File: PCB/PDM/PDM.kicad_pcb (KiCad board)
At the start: 2 copper layers, 196 parts, among them IC1 BTS70021EPPXUMA1, IC1 STM32L496ZGT6, IC10 BTS70021EPPXUMA1, IC11 BTS70021EPPXUMA1, IC12 LM5050MK-1_NOPB, IC13 LM5050MK-1_NOPB, IC14 TLE9104SHXUMA1, IC2 AT25SF128A-SHB-T, IC2 BTS70021EPPXUMA1, IC3 BTS500101TAEATMA1, IC4 TS5A21366DCUR, IC5 TMP126NDCKR, IC6 TMP126NDCKR, IC7 BTS722204ESAXUMA1, IC8 BTS722204ESAXUMA1, IC9 BTS500101TAEATMA1, Q1 MMBT3904, Q2 IAUA250N04S6N007AUMA1, Q3 IAUA250N04S6N007AUMA1, Q4 NDT3055L, U1 STM32L496VGTx, U2 MCP2561-E-SN, U3 MCP2561-E-SN, U4 VNF1048FTR, Y1 48Mhz, Y2 32KHz

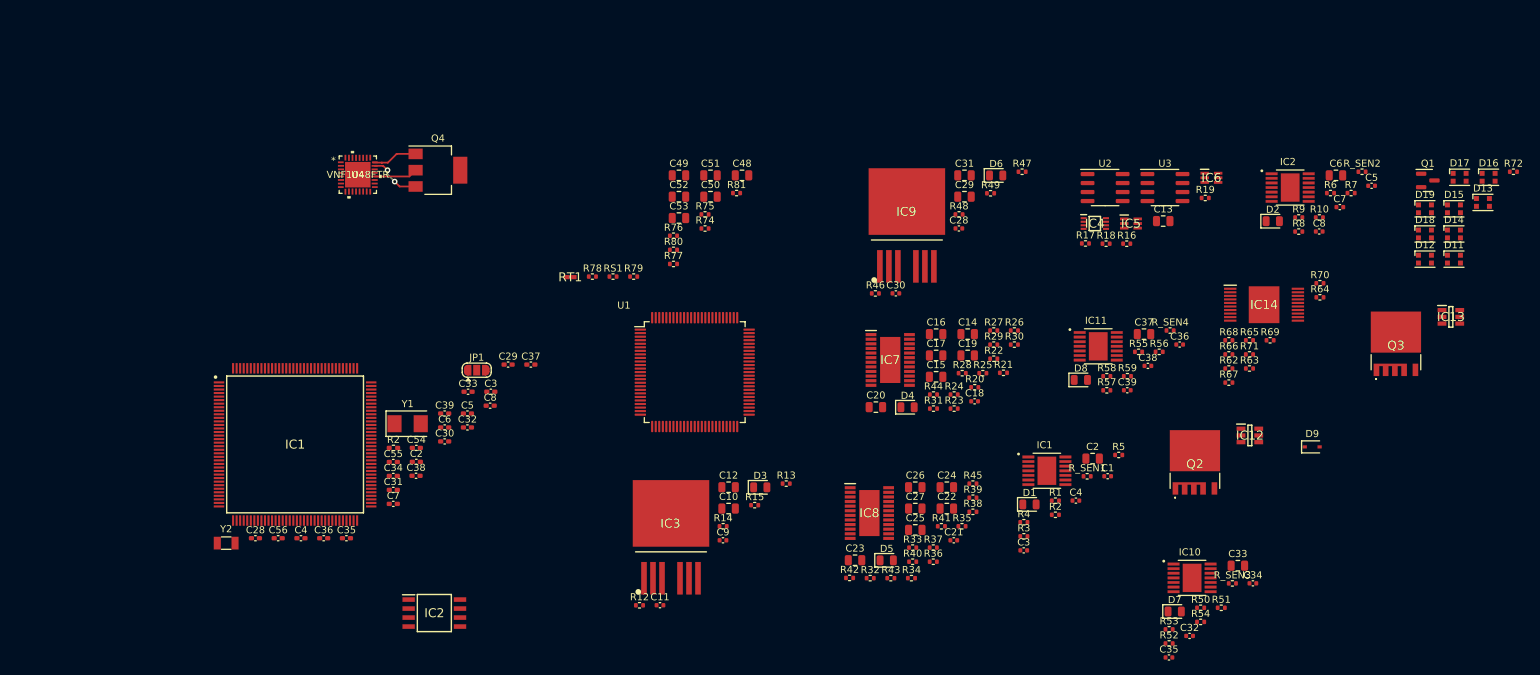
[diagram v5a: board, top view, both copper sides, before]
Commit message: Added new type of high side driver based on VNF1048 + STL135
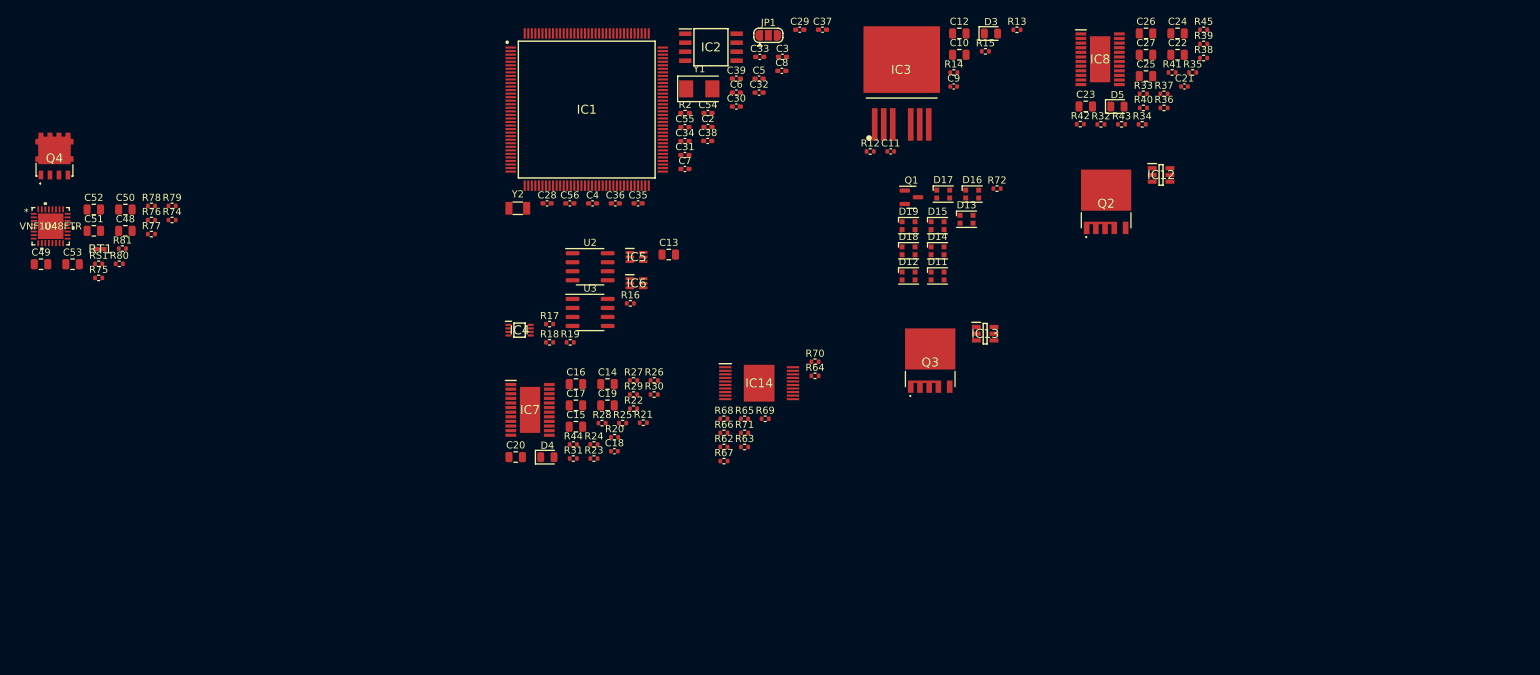
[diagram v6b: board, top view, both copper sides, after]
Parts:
- removed C1: 220pF, Capacitor_SMD:C_0402_1005Metric
- removed the C2 at (187.9, 89.0)
- removed the C2 at (92.5, 89.4)
- removed the C28 at (169.0, 56.5)
- removed the C28 at (69.8, 100.2)
- removed the C29 at (169.8, 52.0)
- removed the C29 at (105.4, 75.7)
- removed the C3 at (178.2, 101.9)
- removed the C3 at (103.0, 79.5)
- removed the C30 at (160.1, 65.6)
- removed the C30 at (96.5, 86.5)
- removed the C31 at (169.8, 49.0)
- removed the C31 at (89.2, 93.4)
- removed the C32 at (99.7, 84.6)
- removed the C32 at (201.6, 114.0)
- removed the C33 at (208.4, 104.1)
- removed the C33 at (99.8, 79.5)
- removed the C34 at (89.2, 91.4)
- removed the C34 at (210.5, 106.5)
- removed the C35 at (198.6, 117.0)
- removed the C35 at (82.6, 100.2)
- removed the C36 at (200.2, 72.9)
- removed the C36 at (79.4, 100.2)
- removed the C37 at (195.1, 71.4)
- removed the C37 at (108.6, 75.7)
- removed the C38 at (195.7, 75.9)
- removed the C38 at (92.4, 91.4)
- removed the C39 at (192.8, 79.3)
- removed the C39 at (96.5, 82.6)
- removed the C4 at (185.5, 94.9)
- removed the C4 at (76.2, 100.2)
- removed the C5 at (227.2, 50.5)
- removed the C5 at (99.7, 82.6)
- removed the C6 at (96.5, 84.6)
- removed the C6 at (222.2, 49.0)
- removed the C7 at (89.2, 95.3)
- removed the C7 at (222.8, 53.5)
- removed the C8 at (219.8, 56.9)
- removed the C8 at (102.9, 81.5)
- removed D1, D2, D7, D8: 7V, Diode_SMD:D_0805_2012Metric
- removed D6: 40V, Diode_SMD:D_0805_2012Metric
- removed D9: 5.1V, Diode_SMD:D_SOD-323
- removed the IC1 at (75.4, 87.0)
- removed the IC1 at (181.4, 90.7)
- removed IC10, IC11: BTS70021EPPXUMA1, PDM_Additional:SOP65P600X115-15N
- removed the IC2 at (215.7, 50.7)
- removed the IC2 at (95.0, 110.7)
- removed IC9: BTS500101TAEATMA1, PDM_Additional:PG-TO263-7-3_3
- removed R1, R50, R55, R6: 4,7k, Resistor_SMD:R_0402_1005Metric
- removed R10, R5, R54, R59: 47, Resistor_SMD:R_0402_1005Metric
- removed the R2 at (89.2, 87.4)
- removed the R2 at (182.6, 96.9)
- removed R3, R4, R46, R48, R51, R52, R53, R56, R57, R58, R7, R8, R9: 4.7k, Resistor_SMD:R_0402_1005Metric
- removed R47: 1k, Resistor_SMD:R_0402_1005Metric
- removed R49: 10, Resistor_SMD:R_0402_1005Metric
- removed R_SEN1, R_SEN2, R_SEN3, R_SEN4: 1.2k, Resistor_SMD:R_0402_1005Metric
- removed U1: STM32L496VGTx, Package_QFP:LQFP-100_14x14mm_P0.5mm
- added C2: 4u7, Capacitor_SMD:C_0402_1005Metric_Pad0.74x0.62mm_HandSolder, F.Cu at (133.6, 42.2)
- added C28: 100n, Capacitor_SMD:C_0402_1005Metric_Pad0.74x0.62mm_HandSolder, F.Cu at (110.9, 52.9)
- added C29: 100n, Capacitor_SMD:C_0402_1005Metric_Pad0.74x0.62mm_HandSolder, F.Cu at (146.6, 28.4)
- added C3: 10pF, Capacitor_SMD:C_0402_1005Metric_Pad0.74x0.62mm_HandSolder, F.Cu at (144.1, 32.3)
- added C30: 100n, Capacitor_SMD:C_0402_1005Metric_Pad0.74x0.62mm_HandSolder, F.Cu at (137.6, 39.3)
- added C31: 100n, Capacitor_SMD:C_0402_1005Metric_Pad0.74x0.62mm_HandSolder, F.Cu at (130.4, 46.1)
- added C32: 100n, Capacitor_SMD:C_0402_1005Metric_Pad0.74x0.62mm_HandSolder, F.Cu at (140.8, 37.3)
- added C33: 100n, Capacitor_SMD:C_0402_1005Metric_Pad0.74x0.62mm_HandSolder, F.Cu at (140.9, 32.3)
- added C34: 100n, Capacitor_SMD:C_0402_1005Metric_Pad0.74x0.62mm_HandSolder, F.Cu at (130.4, 44.2)
- added C35: 100n, Capacitor_SMD:C_0402_1005Metric_Pad0.74x0.62mm_HandSolder, F.Cu at (123.7, 52.9)
- added C36: 100n, Capacitor_SMD:C_0402_1005Metric_Pad0.74x0.62mm_HandSolder, F.Cu at (120.5, 52.9)
- added C37: 100n, Capacitor_SMD:C_0402_1005Metric_Pad0.74x0.62mm_HandSolder, F.Cu at (149.8, 28.4)
- added C38: 100n, Capacitor_SMD:C_0402_1005Metric_Pad0.74x0.62mm_HandSolder, F.Cu at (133.6, 44.1)
- added C39: 100n, Capacitor_SMD:C_0402_1005Metric_Pad0.74x0.62mm_HandSolder, F.Cu at (137.6, 35.3)
- added C4: 1u, Capacitor_SMD:C_0402_1005Metric_Pad0.74x0.62mm_HandSolder, F.Cu at (117.3, 52.9)
- added C5: 100n, Capacitor_SMD:C_0402_1005Metric_Pad0.74x0.62mm_HandSolder, F.Cu at (140.8, 35.3)
- added C6: 100n, Capacitor_SMD:C_0402_1005Metric_Pad0.74x0.62mm_HandSolder, F.Cu at (137.6, 37.3)
- added C7: 10pF, Capacitor_SMD:C_0402_1005Metric_Pad0.74x0.62mm_HandSolder, F.Cu at (130.4, 48.1)
- added C8: 100n, Capacitor_SMD:C_0402_1005Metric_Pad0.74x0.62mm_HandSolder, F.Cu at (144.0, 34.2)
- added IC1: STM32L496ZGT6, PDM_Additional:QFP50P2200X2200X160-144N, F.Cu at (116.5, 39.7)
- added IC2: AT25SF128A-SHB-T, PDM_Additional:SOIC127P798X216-8N, F.Cu at (134.0, 30.9)
- added R2: 1k, Resistor_SMD:R_0402_1005Metric_Pad0.72x0.64mm_HandSolder, F.Cu at (130.4, 40.2)
- Q4: value NDT3055L -> STL135N8F7AG; footprint Package_TO_SOT_SMD:SOT-223-3_TabPin2 -> PDM_Additional:STL135N8F7AG
- moved R19 91.9 mm to (114.2, 72.6)
- moved C49 90.9 mm to (39.5, 61.5)
- moved C48 87.4 mm to (51.4, 56.8)
- moved C51 87.4 mm to (47.0, 56.8)
- moved R81 87.0 mm to (51.0, 59.3)
- moved R75 86.0 mm to (47.6, 63.5)
- moved C53 85.8 mm to (44.0, 61.5)
- moved U3 83.0 mm to (117.0, 68.3)
- moved C52 82.6 mm to (47.0, 53.8)
- moved C50 82.6 mm to (51.4, 53.8)
- moved IC4 82.5 mm to (107.0, 70.8)
- moved IC6 82.5 mm to (123.5, 64.2)
- moved R18 79.7 mm to (111.3, 72.6)
- moved R80 78.2 mm to (50.5, 61.5)
- moved R17 76.5 mm to (111.3, 70.0)
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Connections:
- D11 pad 4: /user_peripheral/STATUS_LED_D -> /MCU/PWM_OUT1
- Q4 pad 1: /VNF1048FTR/MOS_GATE -> /VNF1048FTR/MOS_OUT
- Q4 pad 2: /VNF1048FTR/MOS_IN -> /VNF1048FTR/MOS_OUT
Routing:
- net /VNF1048FTR/MOS_OUT: track 7.33 -> 0.00 mm, vias 2 -> 0
- net /VNF1048FTR/MOS_GATE: track 6.51 -> 0.00 mm
- net /VNF1048FTR/MOS_IN: track 6.14 -> 0.00 mm

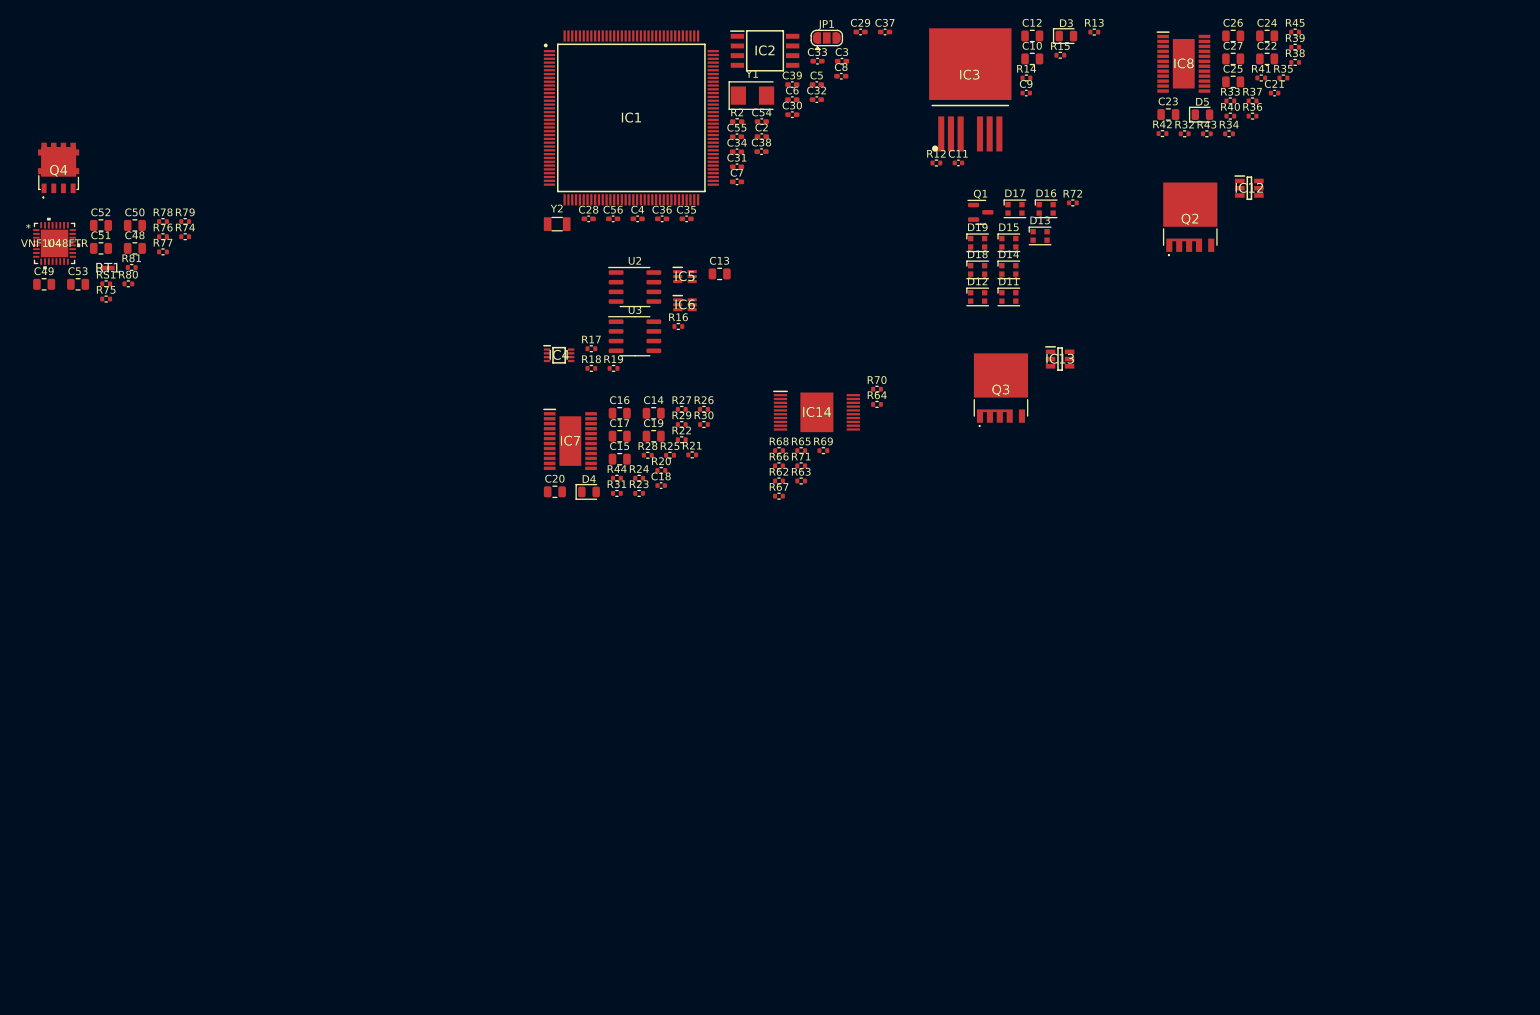
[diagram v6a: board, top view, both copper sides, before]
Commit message: Finished high side section & fixed some ERC's errors
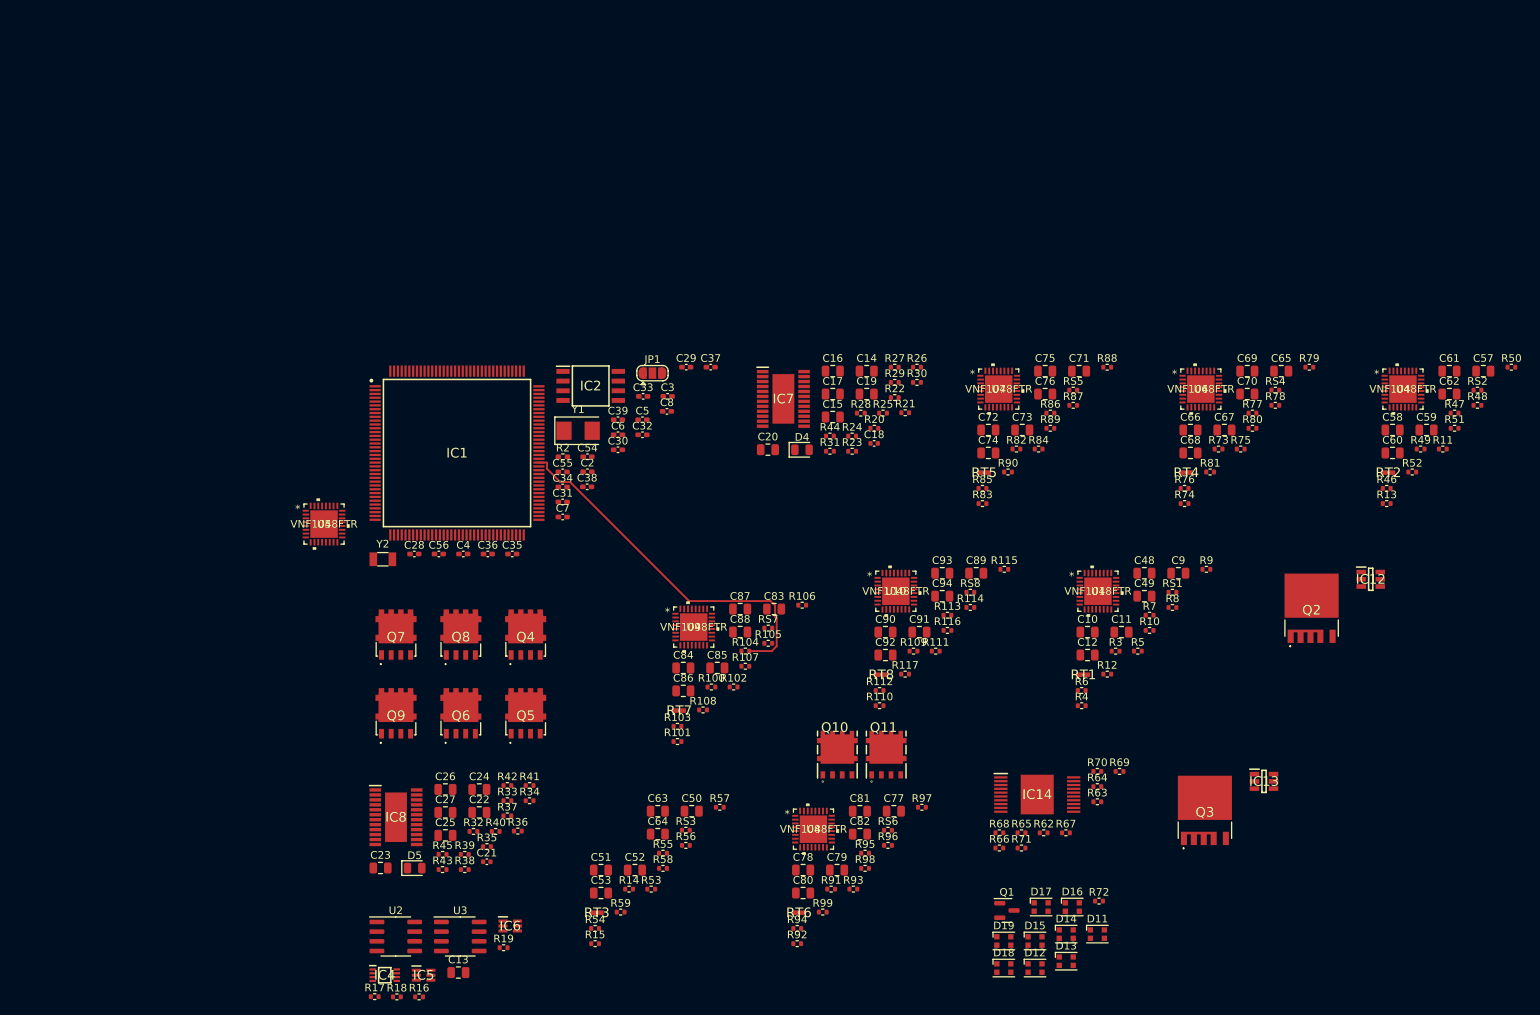
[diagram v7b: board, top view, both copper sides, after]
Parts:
- removed D3: 40V, Diode_SMD:D_0805_2012Metric
- removed IC3: BTS500101TAEATMA1, PDM_Additional:PG-TO263-7-3_3
- added C57: 1uF, Capacitor_SMD:C_0805_2012Metric, F.Cu at (228.2, 72.9)
- added C58: 470nF, Capacitor_SMD:C_0805_2012Metric, F.Cu at (216.3, 80.6)
- added C59: 470nF, Capacitor_SMD:C_0805_2012Metric, F.Cu at (220.8, 80.6)
- added C60: 470nF, Capacitor_SMD:C_0805_2012Metric, F.Cu at (216.3, 83.6)
- added C61: 20uF, Capacitor_SMD:C_0805_2012Metric, F.Cu at (223.8, 72.9)
- added C62: 100nF, Capacitor_SMD:C_0805_2012Metric, F.Cu at (223.8, 75.9)
- added C63: 20uF, Capacitor_SMD:C_0805_2012Metric, F.Cu at (120.0, 130.6)
- added C64: 100nF, Capacitor_SMD:C_0805_2012Metric, F.Cu at (120.0, 133.6)
- added C65: 1uF, Capacitor_SMD:C_0805_2012Metric, F.Cu at (201.7, 72.9)
- added C66: 470nF, Capacitor_SMD:C_0805_2012Metric, F.Cu at (189.8, 80.6)
- added C67: 470nF, Capacitor_SMD:C_0805_2012Metric, F.Cu at (194.3, 80.6)
- added C68: 470nF, Capacitor_SMD:C_0805_2012Metric, F.Cu at (189.8, 83.6)
- added C69: 20uF, Capacitor_SMD:C_0805_2012Metric, F.Cu at (197.3, 72.9)
- added C70: 100nF, Capacitor_SMD:C_0805_2012Metric, F.Cu at (197.3, 75.9)
- added C71: 1uF, Capacitor_SMD:C_0805_2012Metric, F.Cu at (175.2, 72.9)
- added C72: 470nF, Capacitor_SMD:C_0805_2012Metric, F.Cu at (163.3, 80.6)
- added C73: 470nF, Capacitor_SMD:C_0805_2012Metric, F.Cu at (167.8, 80.6)
- added C74: 470nF, Capacitor_SMD:C_0805_2012Metric, F.Cu at (163.3, 83.6)
- added C75: 20uF, Capacitor_SMD:C_0805_2012Metric, F.Cu at (170.8, 72.9)
- added C76: 100nF, Capacitor_SMD:C_0805_2012Metric, F.Cu at (170.8, 75.9)
- added C77: 1uF, Capacitor_SMD:C_0805_2012Metric, F.Cu at (150.9, 130.6)
- added C78: 470nF, Capacitor_SMD:C_0805_2012Metric, F.Cu at (139.0, 138.3)
- added C79: 470nF, Capacitor_SMD:C_0805_2012Metric, F.Cu at (143.5, 138.3)
- added C80: 470nF, Capacitor_SMD:C_0805_2012Metric, F.Cu at (139.0, 141.3)
- added C81: 20uF, Capacitor_SMD:C_0805_2012Metric, F.Cu at (146.5, 130.6)
- added C82: 100nF, Capacitor_SMD:C_0805_2012Metric, F.Cu at (146.5, 133.6)
- added C83: 1uF, Capacitor_SMD:C_0805_2012Metric, F.Cu at (135.2, 104.1)
- added C84: 470nF, Capacitor_SMD:C_0805_2012Metric, F.Cu at (123.3, 111.8)
- added C85: 470nF, Capacitor_SMD:C_0805_2012Metric, F.Cu at (127.8, 111.8)
- added C86: 470nF, Capacitor_SMD:C_0805_2012Metric, F.Cu at (123.3, 114.8)
- added C87: 20uF, Capacitor_SMD:C_0805_2012Metric, F.Cu at (130.8, 104.1)
- added C88: 100nF, Capacitor_SMD:C_0805_2012Metric, F.Cu at (130.8, 107.1)
- added C89: 1uF, Capacitor_SMD:C_0805_2012Metric, F.Cu at (161.7, 99.4)
- added C90: 470nF, Capacitor_SMD:C_0805_2012Metric, F.Cu at (149.8, 107.1)
- added C91: 470nF, Capacitor_SMD:C_0805_2012Metric, F.Cu at (154.3, 107.1)
- added C92: 470nF, Capacitor_SMD:C_0805_2012Metric, F.Cu at (149.8, 110.1)
- added C93: 20uF, Capacitor_SMD:C_0805_2012Metric, F.Cu at (157.3, 99.4)
- added C94: 100nF, Capacitor_SMD:C_0805_2012Metric, F.Cu at (157.3, 102.4)
- added Q10: STL225N6F7AG, PDM_Additional:POWERFLAT_5X6, F.Cu at (143.5, 123.2)
- added Q11: STL225N6F7AG, PDM_Additional:POWERFLAT_5X6, F.Cu at (149.9, 123.2)
- added Q5: STL135N8F7AG, PDM_Additional:STL135N8F7AG, F.Cu at (102.6, 117.6)
- added Q6: STL135N8F7AG, PDM_Additional:STL135N8F7AG, F.Cu at (94.1, 117.6)
- added Q7: STL135N8F7AG, PDM_Additional:STL135N8F7AG, F.Cu at (85.6, 107.3)
- added Q8: STL135N8F7AG, PDM_Additional:STL135N8F7AG, F.Cu at (94.1, 107.3)
- added Q9: STL135N8F7AG, PDM_Additional:STL135N8F7AG, F.Cu at (85.6, 117.6)
- added R10: 10k, Resistor_SMD:R_0402_1005Metric, F.Cu at (184.4, 106.9)
- added R100: 1.2k, Resistor_SMD:R_0402_1005Metric, F.Cu at (127.0, 114.3)
- added R101: 4.7k, Resistor_SMD:R_0402_1005Metric, F.Cu at (122.5, 121.5)
- added R102: 1.2k, Resistor_SMD:R_0402_1005Metric, F.Cu at (129.9, 114.3)
- added R103: 1.2k, Resistor_SMD:R_0402_1005Metric, F.Cu at (122.5, 119.5)
- added R104: 1.2k, Resistor_SMD:R_0402_1005Metric, F.Cu at (131.4, 109.6)
- added R105: 1.2k, Resistor_SMD:R_0402_1005Metric, F.Cu at (134.4, 108.6)
- added R106: 1.2k, Resistor_SMD:R_0402_1005Metric, F.Cu at (138.9, 103.6)
- added R107: 10k, Resistor_SMD:R_0402_1005Metric, F.Cu at (131.4, 111.6)
- added R108: 47k, Resistor_SMD:R_0402_1005Metric, F.Cu at (125.9, 117.3)
- added R109: 1.2k, Resistor_SMD:R_0402_1005Metric, F.Cu at (153.5, 109.6)
- added R11: 1.2k, Resistor_SMD:R_0402_1005Metric, F.Cu at (222.9, 83.1)
- added R110: 4.7k, Resistor_SMD:R_0402_1005Metric, F.Cu at (149.0, 116.8)
- added R111: 1.2k, Resistor_SMD:R_0402_1005Metric, F.Cu at (156.4, 109.6)
- added R112: 1.2k, Resistor_SMD:R_0402_1005Metric, F.Cu at (149.0, 114.8)
- added R113: 1.2k, Resistor_SMD:R_0402_1005Metric, F.Cu at (157.9, 104.9)
- added R114: 1.2k, Resistor_SMD:R_0402_1005Metric, F.Cu at (160.9, 103.9)
- added R115: 1.2k, Resistor_SMD:R_0402_1005Metric, F.Cu at (165.4, 98.9)
- added R116: 10k, Resistor_SMD:R_0402_1005Metric, F.Cu at (157.9, 106.9)
- added R117: 47k, Resistor_SMD:R_0402_1005Metric, F.Cu at (152.4, 112.6)
- added R3: 1.2k, Resistor_SMD:R_0402_1005Metric, F.Cu at (180.0, 109.6)
- added R4: 4.7k, Resistor_SMD:R_0402_1005Metric, F.Cu at (175.5, 116.8)
- added R46: 1.2k, Resistor_SMD:R_0402_1005Metric, F.Cu at (215.5, 88.3)
- added R47: 1.2k, Resistor_SMD:R_0402_1005Metric, F.Cu at (224.4, 78.4)
- added R48: 1.2k, Resistor_SMD:R_0402_1005Metric, F.Cu at (227.4, 77.4)
- added R49: 1.2k, Resistor_SMD:R_0402_1005Metric, F.Cu at (220.0, 83.1)
- added R5: 1.2k, Resistor_SMD:R_0402_1005Metric, F.Cu at (182.9, 109.6)
- added R50: 1.2k, Resistor_SMD:R_0402_1005Metric, F.Cu at (231.9, 72.4)
- added R51: 10k, Resistor_SMD:R_0402_1005Metric, F.Cu at (224.4, 80.4)
- added R52: 47k, Resistor_SMD:R_0402_1005Metric, F.Cu at (218.9, 86.1)
- added R53: 1.2k, Resistor_SMD:R_0402_1005Metric, F.Cu at (119.1, 140.8)
- added R54: 1.2k, Resistor_SMD:R_0402_1005Metric, F.Cu at (111.7, 146.0)
- added R55: 1.2k, Resistor_SMD:R_0402_1005Metric, F.Cu at (120.6, 136.1)
- added R56: 1.2k, Resistor_SMD:R_0402_1005Metric, F.Cu at (123.6, 135.1)
- added R57: 1.2k, Resistor_SMD:R_0402_1005Metric, F.Cu at (128.1, 130.1)
- added R58: 10k, Resistor_SMD:R_0402_1005Metric, F.Cu at (120.6, 138.1)
- added R59: 47k, Resistor_SMD:R_0402_1005Metric, F.Cu at (115.1, 143.8)
- added R6: 1.2k, Resistor_SMD:R_0402_1005Metric, F.Cu at (175.5, 114.8)
- added R7: 1.2k, Resistor_SMD:R_0402_1005Metric, F.Cu at (184.4, 104.9)
- added R73: 1.2k, Resistor_SMD:R_0402_1005Metric, F.Cu at (193.5, 83.1)
- added R8: 1.2k, Resistor_SMD:R_0402_1005Metric, F.Cu at (187.4, 103.9)
- added R82: 1.2k, Resistor_SMD:R_0402_1005Metric, F.Cu at (167.0, 83.1)
- added R83: 4.7k, Resistor_SMD:R_0402_1005Metric, F.Cu at (162.5, 90.3)
- added R84: 1.2k, Resistor_SMD:R_0402_1005Metric, F.Cu at (169.9, 83.1)
- added R85: 1.2k, Resistor_SMD:R_0402_1005Metric, F.Cu at (162.5, 88.3)
- added R86: 1.2k, Resistor_SMD:R_0402_1005Metric, F.Cu at (171.4, 78.4)
- added R87: 1.2k, Resistor_SMD:R_0402_1005Metric, F.Cu at (174.4, 77.4)
- added R88: 1.2k, Resistor_SMD:R_0402_1005Metric, F.Cu at (178.9, 72.4)
- added R89: 10k, Resistor_SMD:R_0402_1005Metric, F.Cu at (171.4, 80.4)
- added R9: 1.2k, Resistor_SMD:R_0402_1005Metric, F.Cu at (191.9, 98.9)
- added R90: 47k, Resistor_SMD:R_0402_1005Metric, F.Cu at (165.9, 86.1)
- added R91: 1.2k, Resistor_SMD:R_0402_1005Metric, F.Cu at (142.7, 140.8)
- added R92: 4.7k, Resistor_SMD:R_0402_1005Metric, F.Cu at (138.2, 148.0)
- added R93: 1.2k, Resistor_SMD:R_0402_1005Metric, F.Cu at (145.6, 140.8)
- added R94: 1.2k, Resistor_SMD:R_0402_1005Metric, F.Cu at (138.2, 146.0)
- added R95: 1.2k, Resistor_SMD:R_0402_1005Metric, F.Cu at (147.1, 136.1)
- added R96: 1.2k, Resistor_SMD:R_0402_1005Metric, F.Cu at (150.1, 135.1)
- added R97: 1.2k, Resistor_SMD:R_0402_1005Metric, F.Cu at (154.6, 130.1)
- added R98: 10k, Resistor_SMD:R_0402_1005Metric, F.Cu at (147.1, 138.1)
- added R99: 47k, Resistor_SMD:R_0402_1005Metric, F.Cu at (141.6, 143.8)
- added RS2: 1m, Resistor_SMD:R_0402_1005Metric, F.Cu at (227.4, 75.4)
- added RS3: 1m, Resistor_SMD:R_0402_1005Metric, F.Cu at (123.6, 133.1)
- added RS4: 1m, Resistor_SMD:R_0402_1005Metric, F.Cu at (200.9, 75.4)
- added RS5: 1m, Resistor_SMD:R_0402_1005Metric, F.Cu at (174.4, 75.4)
- added RS6: 1m, Resistor_SMD:R_0402_1005Metric, F.Cu at (150.1, 133.1)
- added RS7: 1m, Resistor_SMD:R_0402_1005Metric, F.Cu at (134.4, 106.6)
- added RS8: 1m, Resistor_SMD:R_0402_1005Metric, F.Cu at (160.9, 101.9)
- added RT2: B57232V5103F360, PDM_Additional:THRMC1005X60N, F.Cu at (215.8, 86.2)
- added RT3: B57232V5103F360, PDM_Additional:THRMC1005X60N, F.Cu at (112.0, 143.9)
- added RT4: B57232V5103F360, PDM_Additional:THRMC1005X60N, F.Cu at (189.3, 86.2)
- added RT5: B57232V5103F360, PDM_Additional:THRMC1005X60N, F.Cu at (162.8, 86.2)
- added RT6: B57232V5103F360, PDM_Additional:THRMC1005X60N, F.Cu at (138.5, 143.9)
- added RT7: B57232V5103F360, PDM_Additional:THRMC1005X60N, F.Cu at (122.8, 117.4)
- added RT8: B57232V5103F360, PDM_Additional:THRMC1005X60N, F.Cu at (149.3, 112.7)
- added U1: VNF1048FTR, PDM_Additional:QFN32L_5x5_STM, F.Cu at (177.7, 101.8)
- added U10: VNF1048FTR, PDM_Additional:QFN32L_5x5_STM, F.Cu at (151.2, 101.8)
- added U5: VNF1048FTR, PDM_Additional:QFN32L_5x5_STM, F.Cu at (76.2, 93.0)
- added U6: VNF1048FTR, PDM_Additional:QFN32L_5x5_STM, F.Cu at (191.2, 75.3)
- added U7: VNF1048FTR, PDM_Additional:QFN32L_5x5_STM, F.Cu at (164.7, 75.3)
- added U8: VNF1048FTR, PDM_Additional:QFN32L_5x5_STM, F.Cu at (140.4, 133.0)
- added U9: VNF1048FTR, PDM_Additional:QFN32L_5x5_STM, F.Cu at (124.7, 106.5)
- C10: value 150nF -> 470nF
- C11: value 10nF -> 470nF; footprint Capacitor_SMD:C_0402_1005Metric -> Capacitor_SMD:C_0805_2012Metric
- C12, C53: value 100nF -> 470nF
- C48: value 1uF -> 20uF
- C49: value 470nF -> 100nF
- C50: value 470nF -> 1uF
- C52: value 20uF -> 470nF
- C9: value 10nF -> 1uF; footprint Capacitor_SMD:C_0402_1005Metric -> Capacitor_SMD:C_0805_2012Metric
- R12: value 4.7k -> 47k
- R13: value 1k -> 4.7k
- R14: value 4.7k -> 1.2k
- R15: value 10 -> 4.7k
- R74: value 1.2k -> 4.7k
- moved U4 177.8 mm to (217.7, 75.3)
- moved R45 155.3 mm to (91.7, 136.3)
- moved R38 151.8 mm to (94.7, 138.3)
- moved R39 151.8 mm to (94.7, 136.3)
- moved R75 150.1 mm to (196.4, 83.1)
- moved C49 149.9 mm to (183.8, 102.4)
- moved R79 148.6 mm to (205.4, 72.4)
- moved R80 148.6 mm to (197.9, 80.4)
- moved R78 147.8 mm to (200.9, 77.4)
- moved RS1 145.5 mm to (187.4, 101.9)
- moved R35 145.1 mm to (97.6, 135.3)
- moved R77 144.4 mm to (197.9, 78.4)
- moved C21 144.3 mm to (97.5, 137.2)
- moved R81 143.9 mm to (192.4, 86.1)
- moved IC8 142.9 mm to (85.6, 131.4)
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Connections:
- net /VNF1048FTR/HWLO renamed /HIGH SIDE1/VNF1048FTR5/HWLO
- net /user_peripheral/BUZZ_IN renamed /USER PERIPHERAL/BUZZ_IN
- C10 pad 1: GND -> +12V
- C11 pad 1: /BTS50010-1TAE/OUT -> Net-(C11-Pad1)
- C11 pad 2: GND -> Net-(C11-Pad2)
- C12 pad 1: /BTS50010-1TAE/VS -> Net-(C12-Pad1)
- C12 pad 2: GND -> Net-(C12-Pad2)
- C48 pad 1: VDD -> +12V
- C48 pad 2: Net-(C48-Pad2) -> GND
- C49 pad 1: /VNF1048FTR/VBAT -> +12V
- C49 pad 2: Net-(C49-Pad2) -> GND
- C50 pad 1: Net-(C50-Pad1) -> VDD
- C51 pad 1: Net-(C51-Pad1) -> +12V
- C52 pad 1: /VNF1048FTR/VBAT -> Net-(C52-Pad1)
- C52 pad 2: GND -> Net-(C52-Pad2)
- C53 pad 1: /VNF1048FTR/VBAT -> Net-(C53-Pad1)
- C53 pad 2: GND -> Net-(C53-Pad2)
- C9 pad 1: /BTS50010-1TAE/ADC -> VDD
- C9 pad 2: GND -> Net-(C9-Pad2)
- IC1 pad 111: /MCU/SCK -> SCK
- IC1 pad 112: /MCU/MISO -> MISO
- IC1 pad 113: /MCU/MOSI -> MOSI
- IC1 pad 115: /MCU/SCK -> SCK
- IC1 pad 117: /MCU/MISO -> MISO
- IC1 pad 118: /MCU/MOSI -> MOSI
- IC1 pad 87: /MCU/SCK -> SCK
- IC1 pad 88: /MCU/MISO -> MISO
- IC1 pad 89: /MCU/MOSI -> MOSI
- Q4 pad 1: /VNF1048FTR/MOS_OUT -> /HIGH SIDE1/VNF1048FTR1/MOS_OUT
- Q4 pad 10: /VNF1048FTR/MOS_IN -> /HIGH SIDE1/VNF1048FTR1/MOS_IN
- Q4 pad 11: /VNF1048FTR/MOS_IN -> /HIGH SIDE1/VNF1048FTR1/MOS_IN
- Q4 pad 12: /VNF1048FTR/MOS_IN -> /HIGH SIDE1/VNF1048FTR1/MOS_IN
- Q4 pad 13: /VNF1048FTR/MOS_IN -> /HIGH SIDE1/VNF1048FTR1/MOS_IN
- Q4 pad 2: /VNF1048FTR/MOS_OUT -> /HIGH SIDE1/VNF1048FTR1/MOS_OUT
- Q4 pad 3: /VNF1048FTR/MOS_OUT -> /HIGH SIDE1/VNF1048FTR1/MOS_OUT
- Q4 pad 4: /VNF1048FTR/MOS_GATE -> /HIGH SIDE1/VNF1048FTR1/MOS_GATE
- Q4 pad 5: /VNF1048FTR/MOS_IN -> /HIGH SIDE1/VNF1048FTR1/MOS_IN
- Q4 pad 6: /VNF1048FTR/MOS_IN -> /HIGH SIDE1/VNF1048FTR1/MOS_IN
- Q4 pad 7: /VNF1048FTR/MOS_IN -> /HIGH SIDE1/VNF1048FTR1/MOS_IN
- Q4 pad 8: /VNF1048FTR/MOS_IN -> /HIGH SIDE1/VNF1048FTR1/MOS_IN
- Q4 pad 9: /VNF1048FTR/MOS_IN -> /HIGH SIDE1/VNF1048FTR1/MOS_IN
- R12 pad 1: /BTS50010-1TAE/ADC -> /HIGH SIDE1/VNF1048FTR1/MOS_OUT
- R12 pad 2: Net-(IC3-Pad3) -> /HIGH SIDE1/VNF1048FTR1/MOS_GATE
- R13 pad 1: Net-(IC3-Pad3) -> Net-(R13-Pad1)
- R13 pad 2: GND -> VDD
- R14 pad 1: /BTS50010-1TAE/IN -> Net-(R14-Pad1)
- R14 pad 2: Net-(C10-Pad2) -> /HIGH SIDE1/VNF1048FTR2/DIAG
- R15 pad 1: GND -> Net-(R14-Pad1)
- R15 pad 2: Net-(IC3-Pad1) -> VDD
- R74 pad 1: Net-(R74-Pad1) -> Net-(R73-Pad1)
- R74 pad 2: /VNF1048FTR/CSN -> VDD
- R75 pad 1: Net-(R75-Pad1) -> /HIGH SIDE1/CSN_SECA5
- R75 pad 2: /VNF1048FTR/SDI -> /HIGH SIDE1/CSN_SECA5
- R76 pad 1: Net-(R76-Pad1) -> MOSI
- R76 pad 2: /VNF1048FTR/SDO -> MOSI
- R77 pad 1: Net-(R77-Pad1) -> MISO
- R77 pad 2: /VNF1048FTR/SCK -> MISO
- R78 pad 1: Net-(R78-Pad1) -> SCK
- R78 pad 2: /VNF1048FTR/DIAG -> SCK
- R81 pad 1: /VNF1048FTR/MOS_OUT -> /HIGH SIDE1/VNF1048FTR5/MOS_OUT
- R81 pad 2: /VNF1048FTR/MOS_GATE -> /HIGH SIDE1/VNF1048FTR5/MOS_GATE
- RS1 pad 1: /VNF1048FTR/VBAT -> +12V
- RS1 pad 2: /VNF1048FTR/MOS_IN -> /HIGH SIDE1/VNF1048FTR1/MOS_IN
- RT1 pad 1: Net-(R80-Pad1) -> Net-(R10-Pad1)
- RT1 pad 2: /VNF1048FTR/MOS_IN -> /HIGH SIDE1/VNF1048FTR1/MOS_IN
- U4 pad 10: Net-(R79-Pad1) -> Net-(R50-Pad1)
- U4 pad 12: Net-(C48-Pad2) -> Net-(C57-Pad2)
- U4 pad 18: Net-(R80-Pad2) -> Net-(R51-Pad2)
- U4 pad 19: Net-(R80-Pad1) -> Net-(R51-Pad1)
- U4 pad 2: Net-(R74-Pad1) -> /HIGH SIDE1/CSN_SECA1
- U4 pad 20: /VNF1048FTR/MOS_IN -> /HIGH SIDE1/VNF1048FTR/MOS_IN
- U4 pad 21: /VNF1048FTR/VBAT -> +12V
- U4 pad 23: /VNF1048FTR/MOS_OUT -> /HIGH SIDE1/VNF1048FTR/MOS_OUT
- U4 pad 24: /VNF1048FTR/MOS_GATE -> /HIGH SIDE1/VNF1048FTR/MOS_GATE
- U4 pad 25: /VNF1048FTR/VBAT -> +12V
- U4 pad 27: Net-(C49-Pad2) -> Net-(C58-Pad2)
- U4 pad 28: Net-(C51-Pad2) -> Net-(C60-Pad2)
- U4 pad 29: Net-(C51-Pad1) -> Net-(C60-Pad1)
- U4 pad 3: Net-(R75-Pad1) -> MOSI
- U4 pad 30: Net-(C50-Pad2) -> Net-(C59-Pad2)
- U4 pad 31: Net-(C50-Pad1) -> Net-(C59-Pad1)
- U4 pad 4: Net-(R76-Pad1) -> MISO
- U4 pad 5: Net-(R77-Pad1) -> SCK
- U4 pad 6: Net-(R78-Pad1) -> Net-(R13-Pad1)
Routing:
- net MISO: track 0.00 -> 48.5 mm
